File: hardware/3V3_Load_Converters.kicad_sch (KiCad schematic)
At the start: 78 parts, among them J23 N/A, J24 N/A, Q28 EPC2016C, Q29 EPC2016C, Q30 EPC2016C, Q31 EPC2016C, Q8 SI2302DDS-T1-GE3, Q9 SI2302DDS-T1-GE3, U21 INA199C3DCKR, U30 LTC3833EUDC#TRPBF, U31 LTC3833EUDC#TRPBF

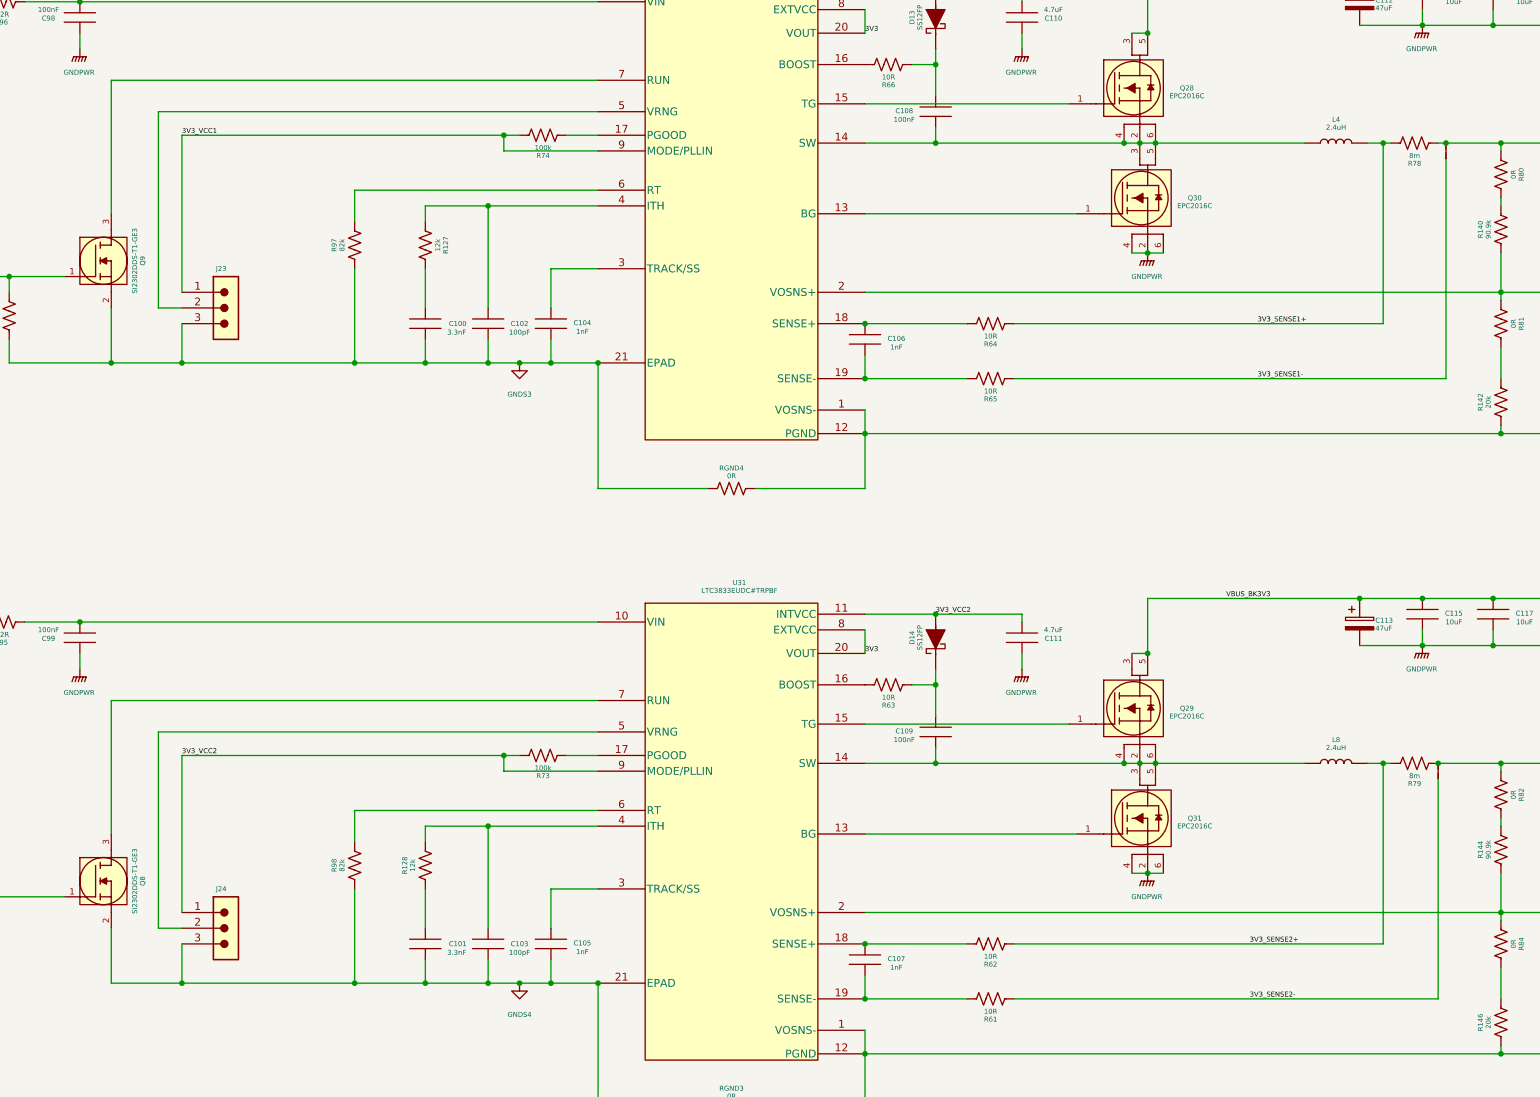
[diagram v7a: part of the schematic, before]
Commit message: hardware: fix some configurations of the LTC3833
Fix the value of the sense resistor of the LTC3833
Fix the jumper configuration used in the LTC3833 to allow the setup of the LTC3833's operating mode.
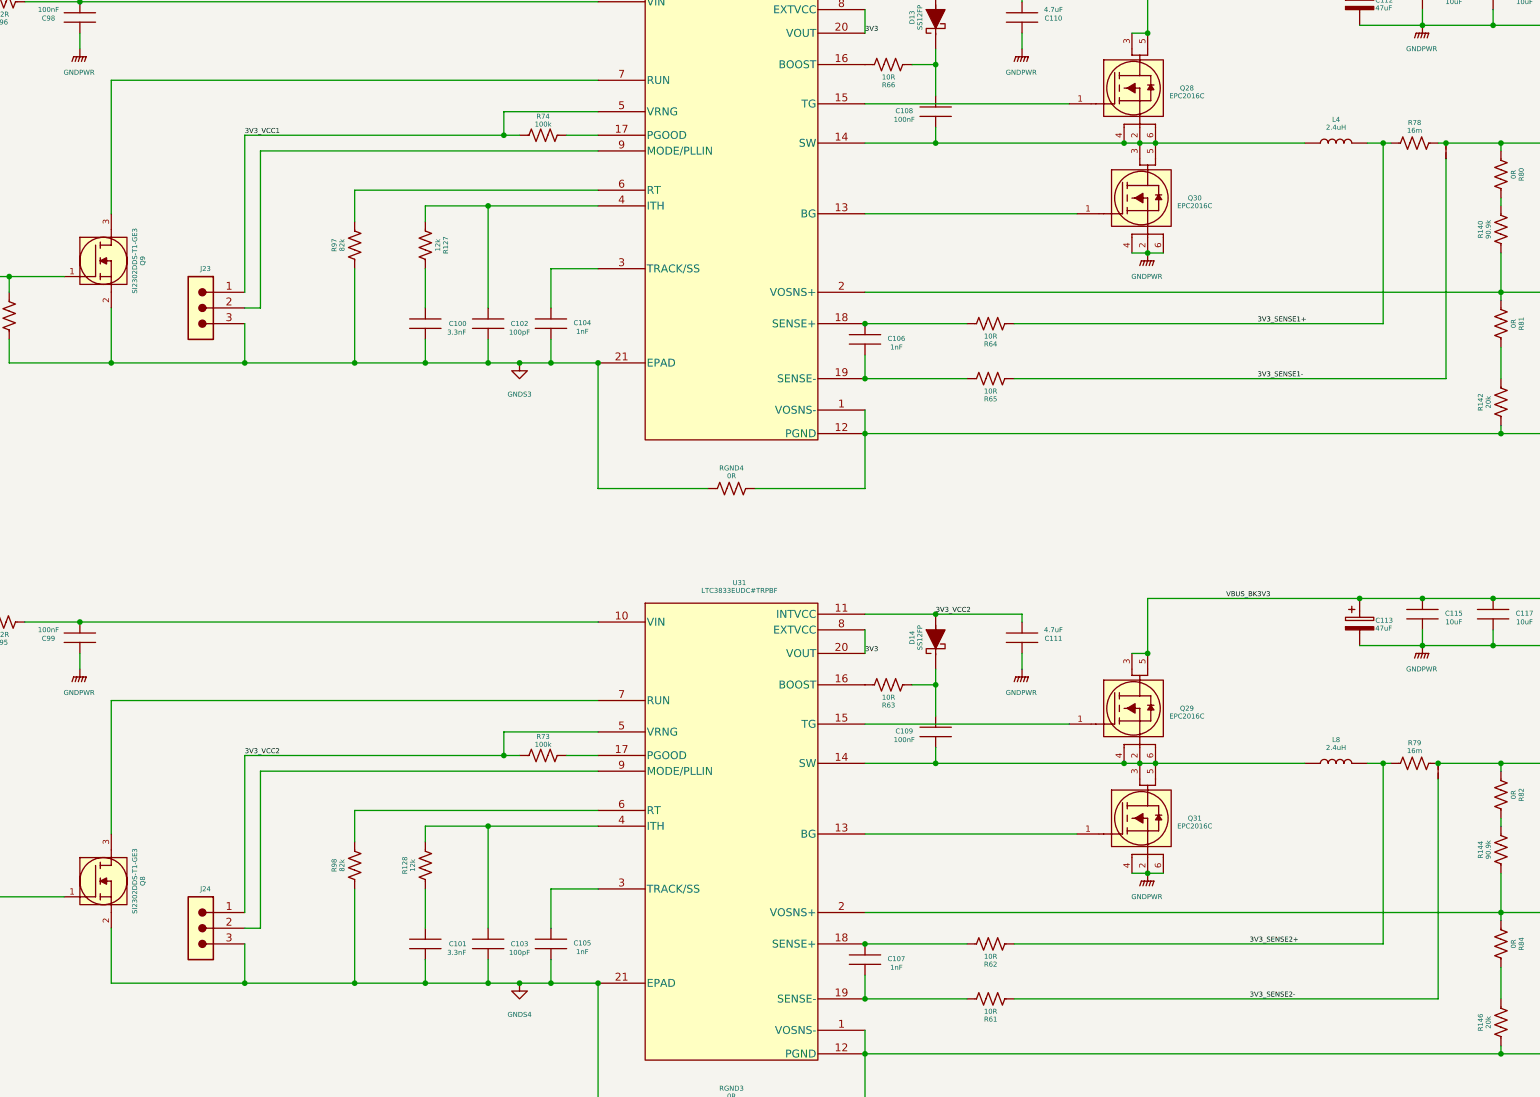
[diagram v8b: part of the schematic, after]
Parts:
- removed R78, R79: 8m, footprints:WSL20108L000FEA18, symbol WSL20108L000FEA18:WSL20108L000FEA18
- added R78, R79: 16m, footprints:WSL2010R0160FEA, symbol WSL2010R0160FEA:WSL2010R0160FEA
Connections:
- net 3V3: now also R78.2, R79.2
- net 3V3_SENSE1+: now also R78.1
- net 3V3_SENSE2+: now also R79.1
- net 3V3_VCC1: now also U30.5 (VRNG); no longer U30.9 (MODE/PLLIN)
- net 3V3_VCC2: now also U31.5 (VRNG); no longer U31.9 (MODE/PLLIN)
- net at J24.2: now also U31.9 (MODE/PLLIN); no longer U31.5 (VRNG)
- net at J23.2: now also U30.9 (MODE/PLLIN); no longer U30.5 (VRNG)
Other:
- moved on the sheet: J23, J24
